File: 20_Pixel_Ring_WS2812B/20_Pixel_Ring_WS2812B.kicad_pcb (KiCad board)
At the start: 2 copper layers, 63.8 x 63.8 mm, 46 parts, among them P1 CONN_01X01, P2 CONN_01X01, P3 CONN_01X01, P4 CONN_01X01, P5 CONN_01X01, P6 CONN_01X01

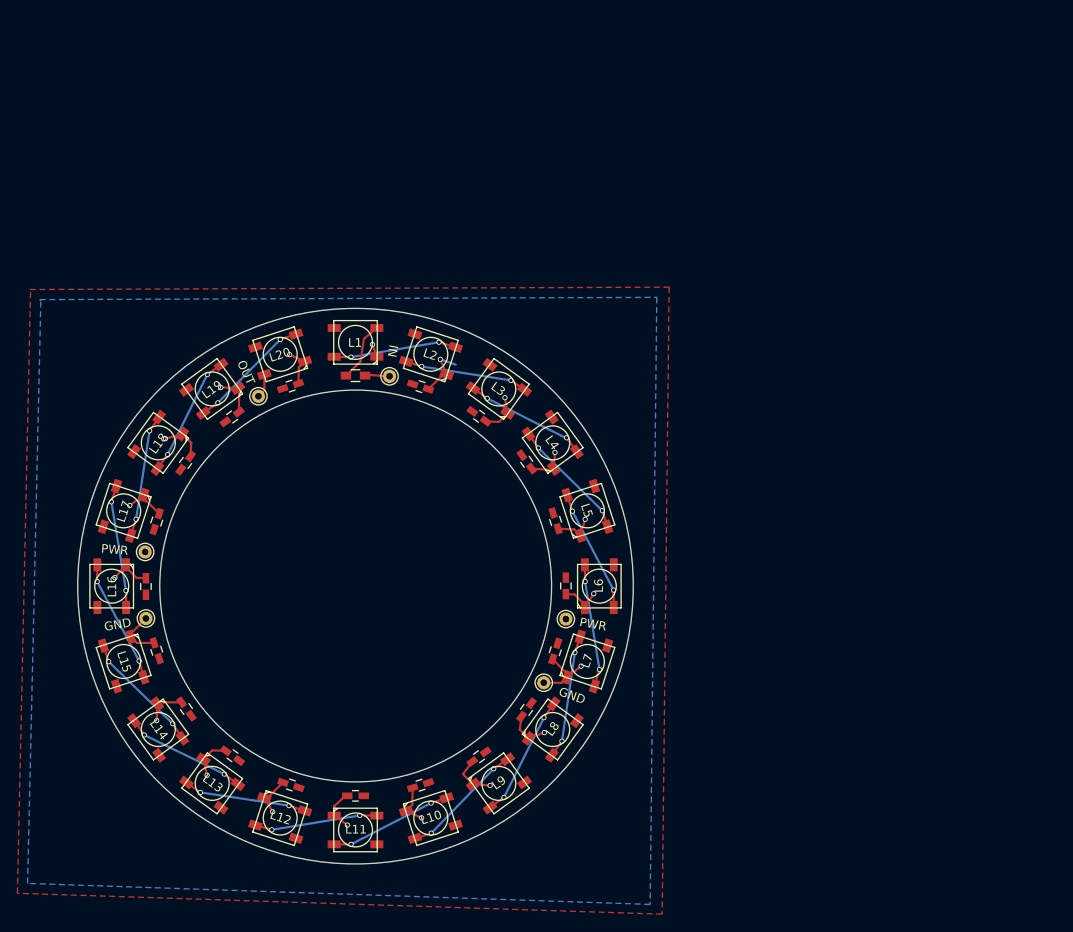
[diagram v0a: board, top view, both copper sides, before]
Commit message: 20 pixel ring updates
Updated / refinements in preparation for nesting the 20 pixel ring
inside the 30 pixel ring for fabrication through OSHPark
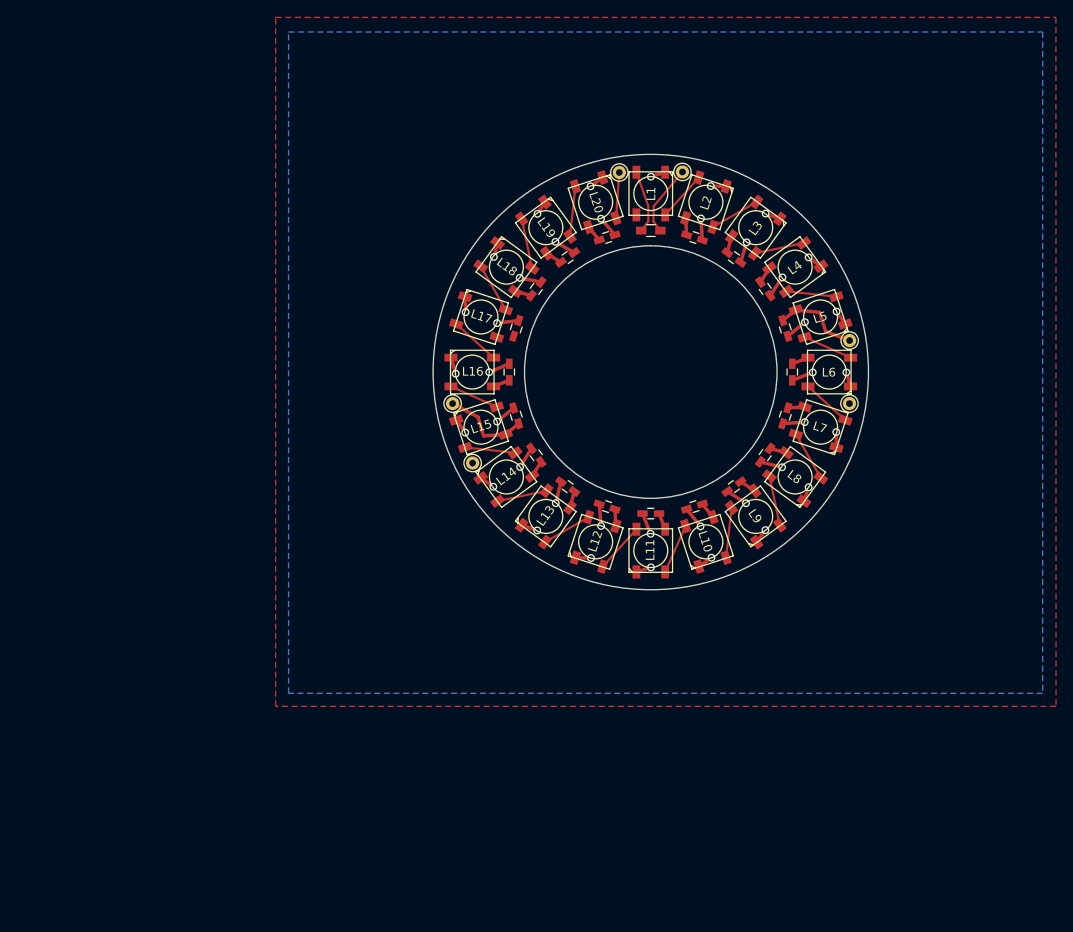
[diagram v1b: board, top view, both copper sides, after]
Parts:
- moved C13 49.6 mm to (164.8, 84.5)
- moved L14 49.4 mm to (161.4, 87.0), turned to 216 degrees
- moved C12 49.4 mm to (168.4, 88.2)
- moved C14 49.3 mm to (162.6, 80.0)
- moved L13 49.1 mm to (165.9, 91.6), turned to 234 degrees
- moved L15 49.1 mm to (158.5, 81.3), turned to 198 degrees
- moved P4 48.8 mm to (174.4, 52.1)
- moved C15 48.5 mm to (161.8, 75.0)
- moved C11 48.4 mm to (173.0, 90.5)
- moved L16 48.2 mm to (157.5, 75.0), turned to 180 degrees
- moved L12 48.2 mm to (171.7, 94.5), turned to 252 degrees
- moved P5 47.5 mm to (200.8, 78.6)
- moved C10 46.9 mm to (178.0, 91.2)
- moved C16 46.9 mm to (162.6, 70.0)
- moved L17 46.7 mm to (158.5, 68.7), turned to 162 degrees
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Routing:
- net +5V: track 0.00 -> 50.9 mm
- net GND: track 99.6 -> 82.8 mm, vias 19 -> 39
- net Net-(L3-Pad2): track 14.3 -> 5.77 mm, vias 2 -> 0
- net Net-(L13-Pad2): track 14.2 -> 5.77 mm, vias 2 -> 0
- net Net-(L2-Pad2): track 14.2 -> 5.78 mm, vias 2 -> 0
- net Net-(L15-Pad2): track 14.2 -> 5.77 mm, vias 2 -> 0
- net Net-(L10-Pad4): track 14.2 -> 5.79 mm, vias 2 -> 0
- net Net-(L7-Pad2): track 14.2 -> 5.78 mm, vias 2 -> 0
- net Net-(L14-Pad2): track 14.2 -> 5.79 mm, vias 2 -> 0
- net Net-(L18-Pad2): track 14.2 -> 5.77 mm, vias 2 -> 0
- net Net-(L12-Pad2): track 14.2 -> 5.78 mm, vias 2 -> 0
- net Net-(L5-Pad2): track 14.2 -> 5.77 mm, vias 2 -> 0
- net Net-(L10-Pad2): track 14.2 -> 5.77 mm, vias 2 -> 0
- net Net-(L4-Pad2): track 14.2 -> 5.79 mm, vias 2 -> 0
- net Net-(L16-Pad2): track 14.2 -> 5.78 mm, vias 2 -> 0
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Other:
- board size 63.8 x 63.8 mm -> 50 x 50 mm
- net class Default: via_dia 0.6 -> 0.9; via_drill 0.4 -> 0.6
- net class Ground added: clearance 0.2, trace_width 0.4, via_dia 0.9, via_drill 0.6
- net class Power added: clearance 0.2, trace_width 0.4, via_dia 0.9, via_drill 0.6
- rule trace_min: 0.2 -> 0.2032
- rule via_min_drill: 0.3 -> 0.508
- rule via_min_size: 0.4 -> 0.889
- board text added: "30 Pixel Ring Inner Diameter ghost"
- board text added: "Circle Center: (178, 75) Circle Outer Diameter: 25 mm Circle Inner Diameter: 14.5 mm"
- board text added: "Exelon"
- board text added: "Rev 1A 2016"
- board text added: "Scott Cherkofsky"
- board text added: "WS2812B LED Ring"
